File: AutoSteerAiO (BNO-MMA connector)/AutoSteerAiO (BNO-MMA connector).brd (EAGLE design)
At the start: 114.3 x 99.1 mm, 85 parts, among them J4 CONNECTOR 1x5 PINS, K4 CB1A-P-12V, U1 VX7805-1000

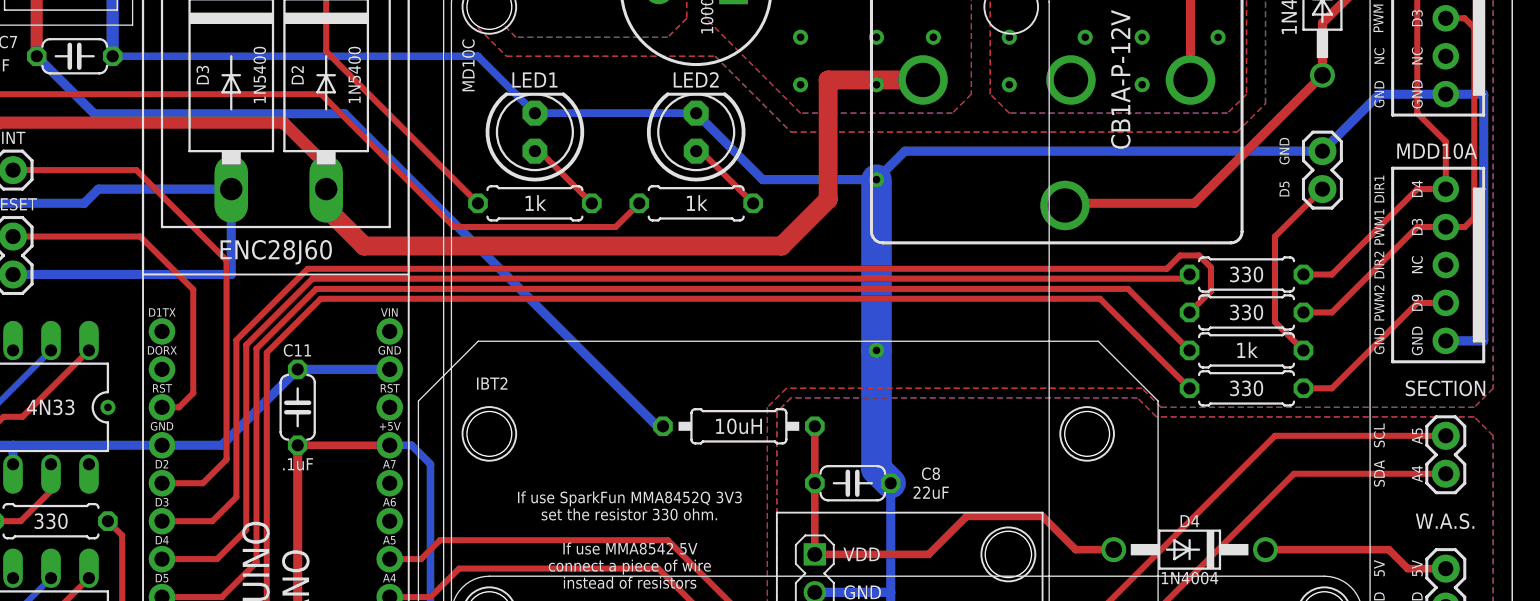
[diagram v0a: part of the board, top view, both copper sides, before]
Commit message: Add files via upload
added led autosteer
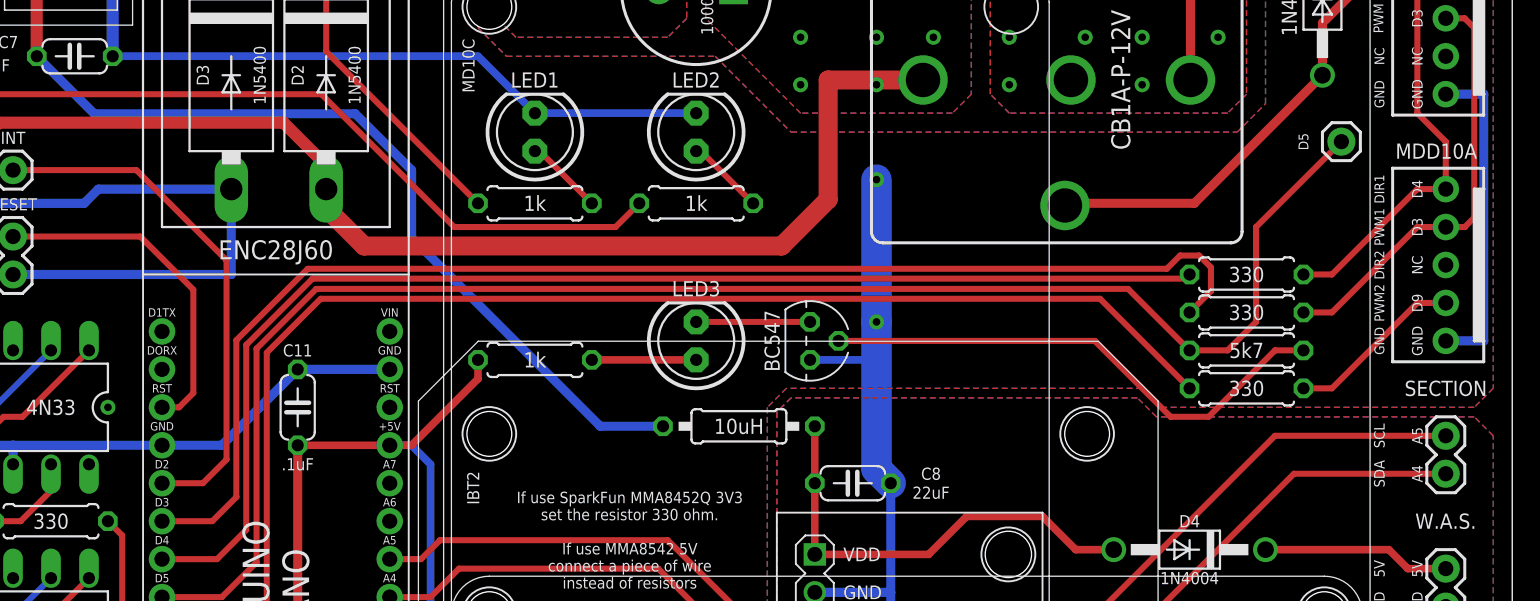
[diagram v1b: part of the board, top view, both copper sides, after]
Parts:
- added LED3: LED, adafruit:LED5MM
- added R21: 1k, resistor:0207/7
- added T1: BC547, transistor:TO92
- D5: device SparkFun-Connectors:1X02 -> SparkFun-Connectors:1X01
- R20: value 1k -> 5k7
- moved D5 3.42 mm to (102.9, 62.9)
- turned R20 to 0 degrees
- renumbered R15 to R20
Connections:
- removed net D5.: D5.1, R20.1
- new net N$23: R20.2, T1.2
- new net N$24: LED3.A, R21.1
- new net N$27: LED3.K, T1.3
- net +5V: now also R21.2
- net D5: now also D5.1, R20.1; no longer R20.2
- net GND: now also T1.1; no longer D5.2
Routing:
- net GND: track 599.4 -> 552.0 mm
- net N$23: track 0.00 -> 35.1 mm
- net D5: track 87.4 -> 107.1 mm
- net D5.: track 12.9 -> 0.00 mm
- net +5V: track 238.4 -> 247.5 mm
- net N$27: track 0.00 -> 7.62 mm
- net N$24: track 0.00 -> 6.98 mm
- net N$25: track 58.5 -> 61.2 mm

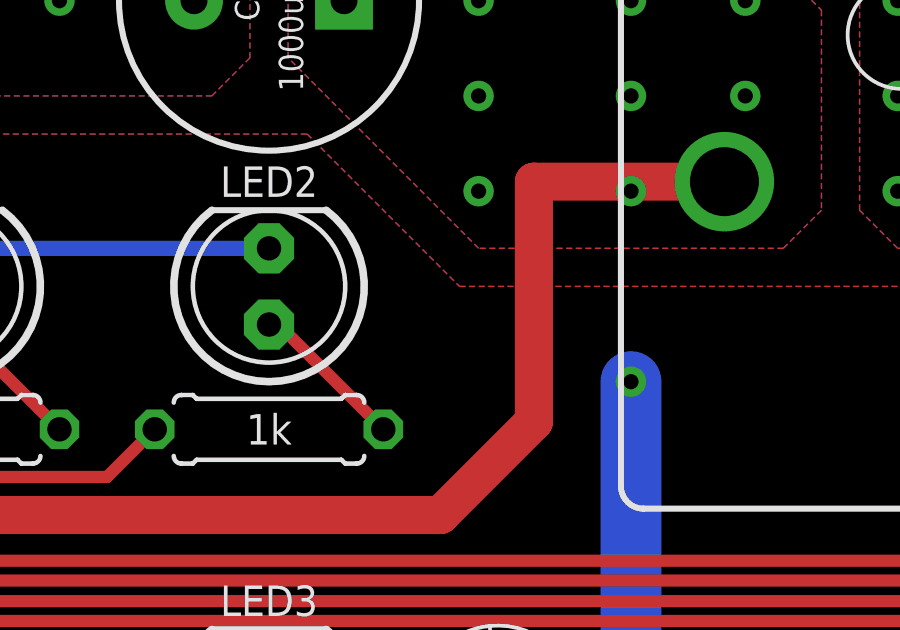
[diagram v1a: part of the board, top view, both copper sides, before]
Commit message: Add files via upload
added led autosteer
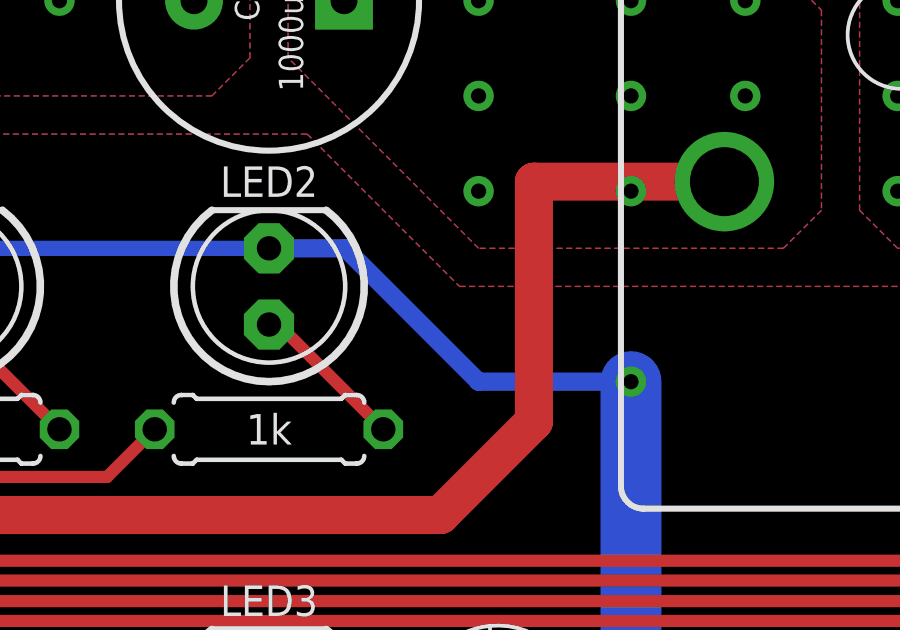
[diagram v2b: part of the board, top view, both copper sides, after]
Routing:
- net GND: track 552.0 -> 565.9 mm
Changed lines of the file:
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@@
 <drawing>
 <settings>
-<setting alwaysvectorfont="yes"/>
+<setting alwaysvectorfont="no"/>
 <setting keepoldvectorfont="yes"/>
 <setting verticaltext="up"/>
@@
 <wire x1="71.755" y1="50.8" x2="71.755" y2="48.26" width="0.508" layer="16"/>
 <wire x1="71.755" y1="50.8" x2="71.755" y2="60.325" width="2.032" layer="16"/>
+<wire x1="71.755" y1="60.325" x2="66.675" y2="60.325" width="0.6096" layer="16"/>
+<wire x1="66.675" y1="60.325" x2="62.23" y2="64.77" width="0.6096" layer="16"/>
+<wire x1="62.23" y1="64.77" x2="59.69" y2="64.77" width="0.6096" layer="16"/>
 </signal>
 <signal name="D5">

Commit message: Add files via upload
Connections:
- net N$25: now also R16.1
- net N$26: no longer R16.1
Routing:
- net N$25: track 61.2 -> 94.8 mm
- net N$26: track 78.1 -> 57.7 mm
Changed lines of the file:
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@@
 <attribute name="CYTRON-PC" value="CN-2600PS-05" x="109.855" y="49.53" size="1.778" layer="27" rot="R90" display="off"/>
 <attribute name="DESC" value="2600 PCB Connector" x="109.855" y="49.53" size="1.778" layer="27" rot="R90" display="off"/>
+<attribute name="LABEL" value="" x="112.776" y="48.133" size="0.762" layer="51" font="vector" ratio="15" rot="R90" align="top-left"/>
 <attribute name="LABEL" value="" x="112.776" y="48.133" size="0.762" layer="21" font="vector" ratio="15" rot="R90" align="top-left"/>
-<attribute name="LABEL" value="" x="112.776" y="48.133" size="0.762" layer="51" font="vector" ratio="15" rot="R90" align="top-left"/>
 <attribute name="LABEL" value="" x="109.855" y="49.53" size="1.778" layer="27" rot="R90" display="off"/>
 <attribute name="MF" value="" x="109.855" y="49.53" size="1.778" layer="27" rot="R90" display="off"/>
@@
 <wire x1="3.7465" y1="9.779" x2="2.54" y2="10.9855" width="0.6096" layer="1"/>
 <wire x1="7.3025" y1="53.975" x2="2.54" y2="49.2125" width="0.6096" layer="1"/>
-<wire x1="43.4975" y1="57.15" x2="34.6075" y2="66.04" width="0.4064" layer="1"/>
-<wire x1="34.6075" y1="66.04" x2="11.43" y2="66.04" width="0.4064" layer="1"/>
+<wire x1="43.4975" y1="57.15" x2="34.925" y2="65.7225" width="0.4064" layer="1"/>
+<wire x1="34.925" y1="65.7225" x2="11.7475" y2="65.7225" width="0.4064" layer="1"/>
 <wire x1="54.2925" y1="57.15" x2="55.88" y2="58.7375" width="0.4064" layer="1"/>
 <wire x1="43.4975" y1="57.15" x2="54.2925" y2="57.15" width="0.4064" layer="1"/>
@@
 <wire x1="5.08" y1="66.5607" x2="5.08" y2="64.77" width="0.8128" layer="1"/>
 <wire x1="8.7122" y1="68.6054" x2="8.8646" y2="68.6054" width="0.4064" layer="1"/>
-<wire x1="8.8646" y1="68.6054" x2="11.43" y2="66.04" width="0.4064" layer="1"/>
+<wire x1="8.8646" y1="68.6054" x2="11.7475" y2="65.7225" width="0.4064" layer="1"/>
 <contactref element="C9" pad="2"/>
 <wire x1="6.731" y1="9.779" x2="12.065" y2="4.445" width="0.6096" layer="1"/>
@@
 <contactref element="C3" pad="2"/>
 <contactref element="C5" pad="+"/>
-<contactref element="R16" pad="1"/>
 <contactref element="PS1" pad="1"/>
 <contactref element="C6" pad="2"/>
@@
 <wire x1="15.5575" y1="80.01" x2="15.555" y2="80.0125" width="0.8128" layer="1"/>
 <wire x1="15.555" y1="80.0125" x2="15.5525" y2="80.01" width="0.8128" layer="1"/>
-<wire x1="34.925" y1="74.93" x2="34.925" y2="68.8975" width="0.4064" layer="1"/>
-<wire x1="45.085" y1="58.7375" x2="34.925" y2="68.8975" width="0.4064" layer="1"/>
 <wire x1="15.5575" y1="90.5275" x2="15.5575" y2="86.36" width="0.8128" layer="1"/>
 <contactref element="U1" pad="1"/>
@@
 <wire x1="19.40175" y1="64.73575" x2="36.86425" y2="64.73575" width="0.6096" layer="16"/>
 <wire x1="40.64" y1="56.4465" x2="53.2715" y2="43.815" width="0.6096" layer="16"/>
+<contactref element="R16" pad="1"/>
+<wire x1="15.5575" y1="68.58" x2="17.145" y2="66.9925" width="0.4064" layer="1"/>
+<wire x1="17.145" y1="66.9925" x2="36.83" y2="66.9925" width="0.4064" layer="1"/>
+<wire x1="45.085" y1="58.7375" x2="36.83" y2="66.9925" width="0.4064" layer="1"/>
 </signal>
 <signal name="N$3">

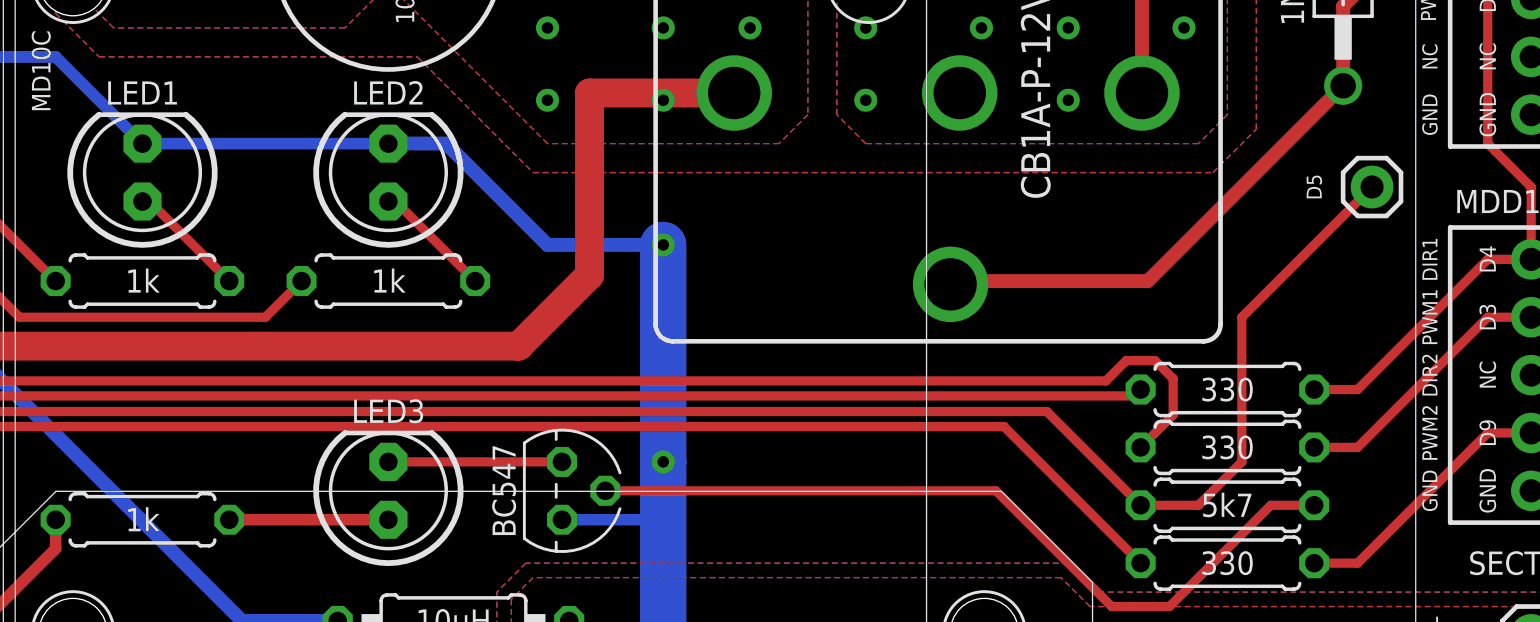
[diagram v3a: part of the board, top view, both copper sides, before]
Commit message: Add files via upload
Adeed 5V connector for IBT2
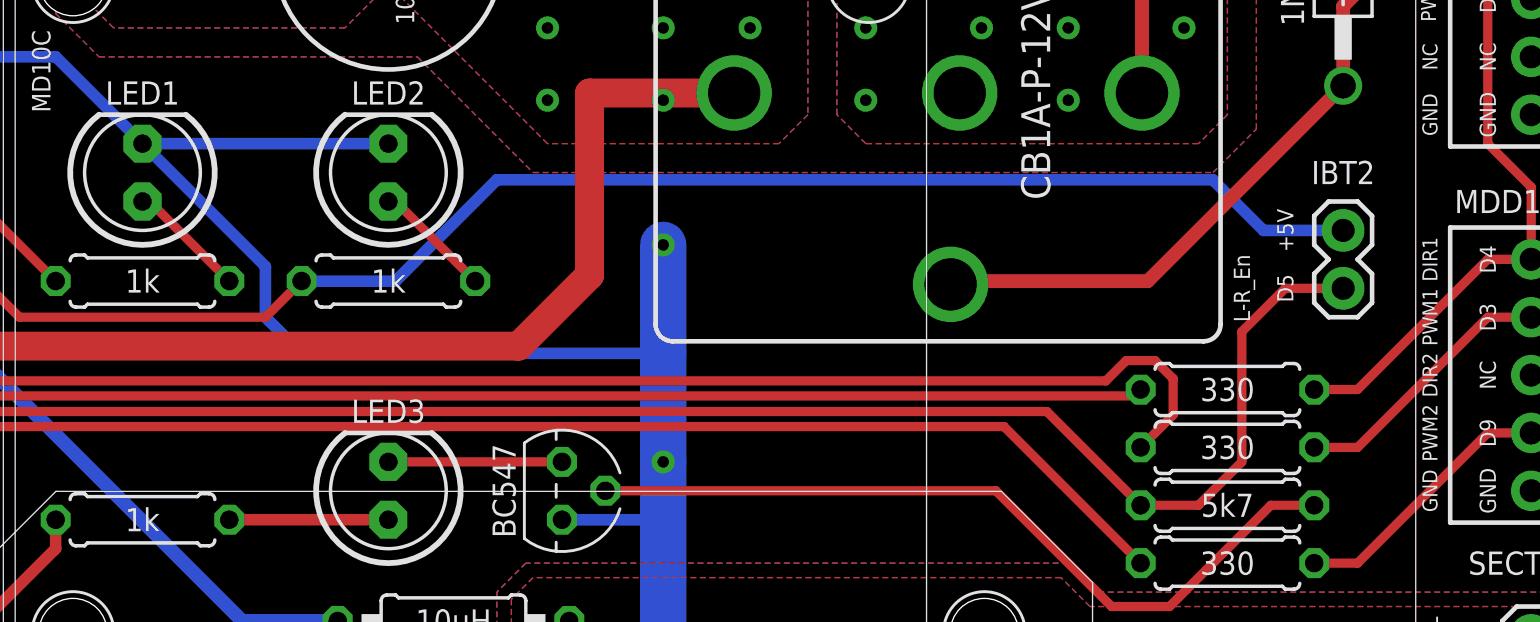
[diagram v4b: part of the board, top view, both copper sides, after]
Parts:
- D5: device SparkFun-Connectors:1X01 -> SparkFun-Connectors:1X02
- moved D5 4.62 mm to (101.6, 58.4)
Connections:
- net +5V: now also D5.2
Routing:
- net +5V: track 247.5 -> 295.9 mm
- net GND: track 565.9 -> 580.0 mm
- net D5: track 107.1 -> 103.6 mm
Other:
- board text added: "L-R_En"
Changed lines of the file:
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@@
 <drawing>
 <settings>
-<setting alwaysvectorfont="no"/>
+<setting alwaysvectorfont="yes"/>
 <setting keepoldvectorfont="yes"/>
 <setting verticaltext="up"/>
@@
 <wire x1="67.6275" y1="49.53" x2="68.58" y2="48.5775" width="0.6096" layer="22"/>
 <wire x1="68.58" y1="50.4825" x2="67.6275" y2="49.53" width="0.6096" layer="22"/>
+<text x="101.6" y="63.5" size="1.016" layer="25" font="vector" ratio="14" rot="R180" align="center">IBT2</text>
+<text x="97.155" y="58.42" size="0.7112" layer="25" font="vector" ratio="15" rot="R270" align="center">L-R_En</text>
+<text x="99.06" y="60.96" size="0.7112" layer="25" font="vector" ratio="15" rot="R270" align="center">+5V</text>
+<wire x1="101.9175" y1="59.69" x2="101.2825" y2="59.69" width="0.6096" layer="22"/>
 </plain>
 <attributes>
@@
 <attribute name="VALUE" x="12.5222" y="67.9704" size="0.8128" layer="25" font="vector" ratio="12" align="center"/>
 </element>
-<element name="D5" library="SparkFun-Connectors" library_urn="urn:adsk.eagle:library:513" package="1X01" package3d_urn="urn:adsk.eagle:package:38028/1" value="CONNECTOR 1x1 PIN" x="102.87" y="62.865" smashed="yes" rot="R90">
-<attribute name="MF" value="" x="102.87" y="62.865" size="1.778" layer="27" rot="R90" display="off"/>
-<attribute name="MPN" value="" x="102.87" y="62.865" size="1.778" layer="27" rot="R90" display="off"/>
-<attribute name="NAME" x="100.33" y="62.865" size="0.6604" layer="25" font="vector" ratio="15" rot="R270" align="center"/>
-<attribute name="OC_NEWARK" value="unknown" x="102.87" y="62.865" size="1.778" layer="27" rot="R90" display="off"/>
-</element>
 <element name="0" library="SparkFun-Connectors" library_urn="urn:adsk.eagle:library:513" package="1X03" package3d_urn="urn:adsk.eagle:package:38063/1" value="CONNECTOR 1x2 PINS" x="53.975" y="4.445" smashed="yes">
 <attribute name="MF" value="" x="53.975" y="4.445" size="1.778" layer="27" display="off"/>
@@
 <attribute name="OC_NEWARK" value="unknown" x="74.93" y="49.53" size="1.778" layer="27" rot="R90" display="off"/>
 </element>
+<element name="D5" library="SparkFun-Connectors" library_urn="urn:adsk.eagle:library:513" package="1X02" package3d_urn="urn:adsk.eagle:package:38039/1" value="CONNECTOR 1x1 PIN" x="101.6" y="58.42" smashed="yes" rot="R90">
+<attribute name="MF" value="" x="101.6" y="58.42" size="1.778" layer="27" rot="R90" display="off"/>
+<attribute name="MPN" value="" x="101.6" y="58.42" size="1.778" layer="27" rot="R90" display="off"/>
+<attribute name="NAME" x="99.06" y="58.42" size="0.7112" layer="25" font="vector" ratio="15" rot="R270" align="center"/>
+<attribute name="OC_NEWARK" value="unknown" x="101.6" y="58.42" size="1.778" layer="27" rot="R90" display="off"/>
+</element>
 </elements>
 <signals>
@@
 <wire x1="45.085" y1="46.99" x2="40.64" y2="42.545" width="0.508" layer="1"/>
 <wire x1="40.64" y1="42.545" x2="39.1795" y2="42.545" width="0.508" layer="1"/>
+<contactref element="D5" pad="2"/>
+<wire x1="101.6" y1="60.96" x2="98.1075" y2="60.96" width="0.508" layer="16"/>
+<wire x1="98.1075" y1="60.96" x2="95.885" y2="63.1825" width="0.508" layer="16"/>
+<wire x1="95.885" y1="63.1825" x2="64.4525" y2="63.1825" width="0.508" layer="16"/>
+<wire x1="64.4525" y1="63.1825" x2="63.5" y2="62.23" width="0.508" layer="16"/>
+<wire x1="60.0075" y1="58.7375" x2="55.88" y2="58.7375" width="0.508" layer="16"/>
+<wire x1="63.5" y1="62.23" x2="60.0075" y2="58.7375" width="0.508" layer="16"/>
 </signal>
 <signal name="SCL">
@@
 <wire x1="67.31" y1="48.26" x2="71.755" y2="48.26" width="0.508" layer="16"/>
 <wire x1="71.755" y1="50.8" x2="71.755" y2="48.26" width="0.508" layer="16"/>
-<wire x1="71.755" y1="50.8" x2="71.755" y2="60.325" width="2.032" layer="16"/>
-<wire x1="71.755" y1="60.325" x2="66.675" y2="60.325" width="0.6096" layer="16"/>
-<wire x1="66.675" y1="60.325" x2="62.23" y2="64.77" width="0.6096" layer="16"/>
-<wire x1="62.23" y1="64.77" x2="59.69" y2="64.77" width="0.6096" layer="16"/>
+<wire x1="71.755" y1="50.8" x2="71.755" y2="55.5625" width="2.032" layer="16"/>
+<wire x1="71.755" y1="55.5625" x2="71.755" y2="60.325" width="2.032" layer="16"/>
+<wire x1="48.895" y1="64.77" x2="54.2925" y2="59.3725" width="0.508" layer="16"/>
+<wire x1="54.2925" y1="59.3725" x2="54.2925" y2="57.15" width="0.508" layer="16"/>
+<wire x1="54.2925" y1="57.15" x2="55.88" y2="55.5625" width="0.508" layer="16"/>
+<wire x1="55.88" y1="55.5625" x2="71.755" y2="55.5625" width="0.508" layer="16"/>
 </signal>
 <signal name="D5">
@@
 <wire x1="34.2646" y1="53.0098" x2="88.5952" y2="53.0098" width="0.4064" layer="1"/>
 <contactref element="R20" pad="1"/>
-<contactref element="D5" pad="1"/>
-<wire x1="102.87" y1="62.865" x2="97.155" y2="57.15" width="0.4064" layer="1"/>
-<wire x1="97.155" y1="57.15" x2="97.155" y2="50.8" width="0.4064" layer="1"/>
+<wire x1="97.155" y1="56.515" x2="97.155" y2="50.8" width="0.4064" layer="1"/>
 <wire x1="88.5952" y1="53.0098" x2="92.71" y2="48.895" width="0.4064" layer="1"/>
 <wire x1="97.155" y1="50.8" x2="95.25" y2="48.895" width="0.4064" layer="1"/>
 <wire x1="92.71" y1="48.895" x2="95.25" y2="48.895" width="0.4064" layer="1"/>
+<contactref element="D5" pad="1"/>
+<wire x1="101.6" y1="58.42" x2="99.06" y2="58.42" width="0.4064" layer="1"/>
+<wire x1="99.06" y1="58.42" x2="97.155" y2="56.515" width="0.4064" layer="1"/>
 </signal>
 <signal name="D6">
